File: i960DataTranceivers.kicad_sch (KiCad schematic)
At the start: 8 parts

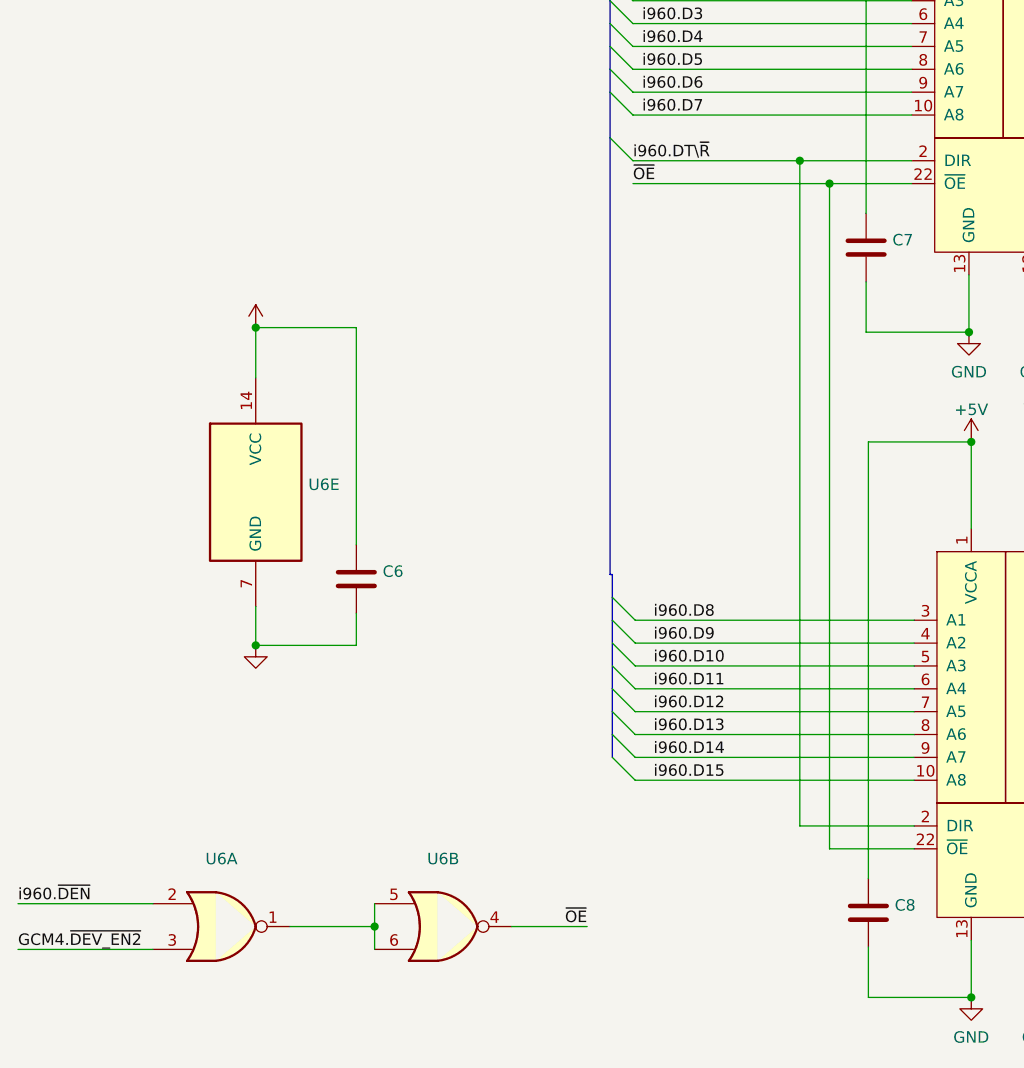
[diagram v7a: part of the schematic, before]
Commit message: Use a third 4809 running independently to act as glue and startup unit.
I was able to remove a nor gate ic by adding. I am also planning to use
the CCLs for other features as well. Perhaps as a simpler inverter.
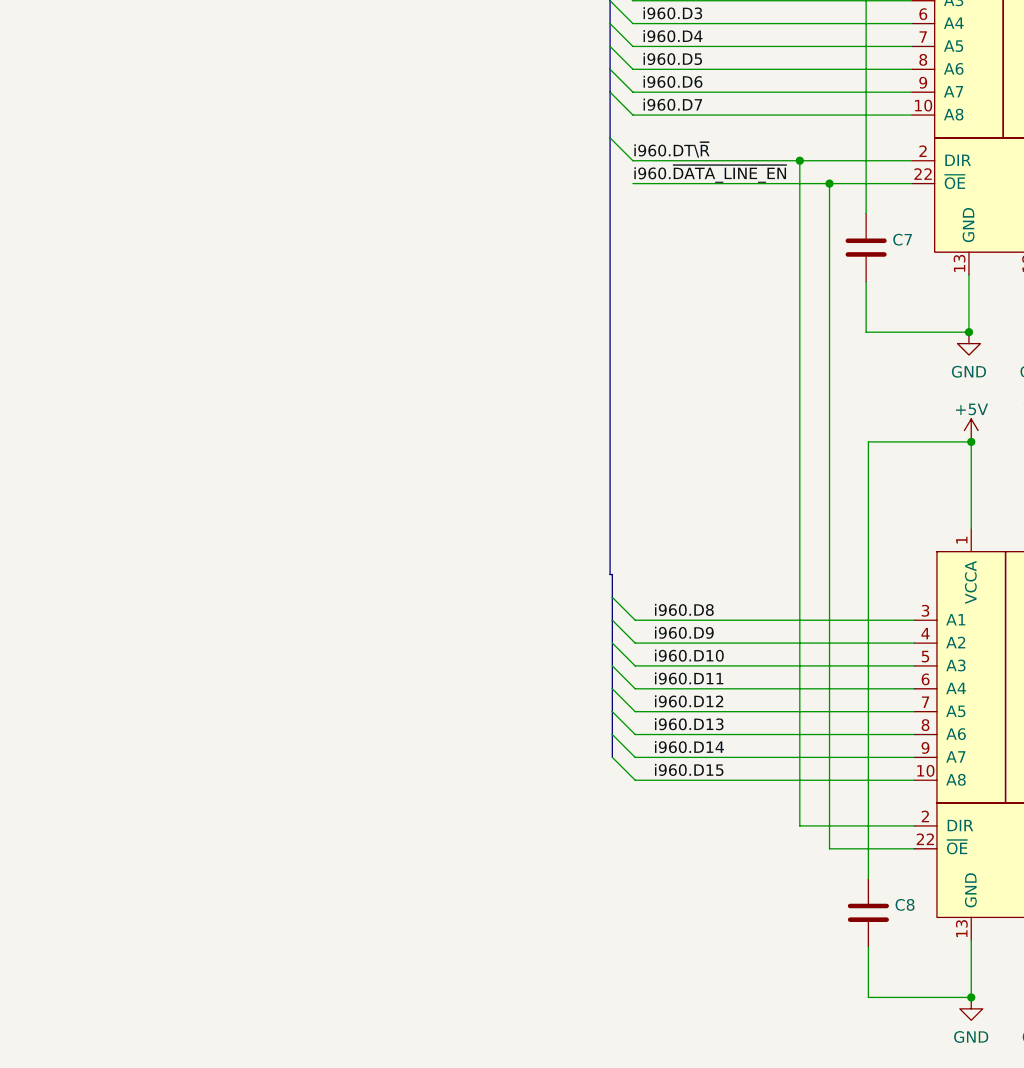
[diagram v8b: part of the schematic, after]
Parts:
- removed C6: (no value), symbol Device:C
- removed U6: (no value), symbol 74xx:74HC02
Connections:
- net ~{OE} renamed i960.~{DATA_LINE_EN}
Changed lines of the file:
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@@
   (junction (at 107.442 70.358) (diameter 0) (color 0 0 0 0)
   )
-  (junction (at 43.688 86.36) (diameter 0) (color 0 0 0 0)
-  )
   (junction (at 130.81 99.06) (diameter 0) (color 0 0 0 0)
   )
@@
   (junction (at 122.936 86.868) (diameter 0) (color 0 0 0 0)
   )
-  (junction (at 56.896 152.908) (diameter 0) (color 0 0 0 0)
-  )
   (junction (at 123.19 160.782) (diameter 0) (color 0 0 0 0)
   )
@@
   (junction (at 123.19 99.06) (diameter 0) (color 0 0 0 0)
   )
-  (junction (at 43.688 121.666) (diameter 0) (color 0 0 0 0)
-  )
   (junction (at 130.556 25.146) (diameter 0) (color 0 0 0 0)
   )
@@
     (stroke (width 0) (type default) (color 0 0 0 0))
   )
-  (wire (pts (xy 56.896 152.908) (xy 56.896 155.448))
-    (stroke (width 0) (type default) (color 0 0 0 0))
-  )
-  (wire (pts (xy 54.864 118.11) (xy 54.864 121.666))
-    (stroke (width 0) (type default) (color 0 0 0 0))
-  )
   (wire (pts (xy 141.732 160.782) (xy 130.81 160.782))
     (stroke (width 0) (type default) (color 0 0 0 0))
@@
     (stroke (width 0) (type default) (color 0 0 0 0))
   )
-  (wire (pts (xy 56.896 152.908) (xy 56.896 150.368))
-    (stroke (width 0) (type default) (color 0 0 0 0))
-  )
   (wire (pts (xy 141.732 99.06) (xy 141.732 147.574))
     (stroke (width 0) (type default) (color 0 0 0 0))
   )
-  (wire (pts (xy 47.498 152.908) (xy 56.896 152.908))
-    (stroke (width 0) (type default) (color 0 0 0 0))
-  )
   (bus (pts (xy 83.058 42.418) (xy 83.058 44.958))
     (stroke (width 0) (type default) (color 0 0 0 0))
@@
     (stroke (width 0) (type default) (color 0 0 0 0))
   )
-  (wire (pts (xy 72.136 152.908) (xy 80.518 152.908))
-    (stroke (width 0) (type default) (color 0 0 0 0))
-  )
   (wire (pts (xy 107.442 70.358) (xy 116.586 70.358))
     (stroke (width 0) (type default) (color 0 0 0 0))
@@
     (stroke (width 0) (type default) (color 0 0 0 0))
   )
-  (wire (pts (xy 54.864 86.36) (xy 54.864 110.49))
-    (stroke (width 0) (type default) (color 0 0 0 0))
-  )
   (wire (pts (xy 137.16 131.572) (xy 168.148 131.572))
     (stroke (width 0) (type default) (color 0 0 0 0))
@@
     (stroke (width 0) (type default) (color 0 0 0 0))
   )
-  (wire (pts (xy 43.688 86.36) (xy 54.864 86.36))
-    (stroke (width 0) (type default) (color 0 0 0 0))
-  )
   (wire (pts (xy 123.19 154.432) (xy 123.19 160.782))
     (stroke (width 0) (type default) (color 0 0 0 0))
@@
     (stroke (width 0) (type default) (color 0 0 0 0))
   )
-  (wire (pts (xy 43.688 91.948) (xy 43.688 86.36))
-    (stroke (width 0) (type default) (color 0 0 0 0))
-  )
   (wire (pts (xy 123.19 99.06) (xy 123.19 108.712))
     (stroke (width 0) (type default) (color 0 0 0 0))
@@
     (stroke (width 0) (type default) (color 0 0 0 0))
   )
-  (wire (pts (xy 17.272 155.448) (xy 32.258 155.448))
-    (stroke (width 0) (type default) (color 0 0 0 0))
-  )
-  (wire (pts (xy 43.688 121.666) (xy 43.688 117.348))
-    (stroke (width 0) (type default) (color 0 0 0 0))
-  )
-  (wire (pts (xy 54.864 121.666) (xy 43.688 121.666))
-    (stroke (width 0) (type default) (color 0 0 0 0))
-  )
   (bus (pts (xy 83.058 57.658) (xy 83.058 60.198))
     (stroke (width 0) (type default) (color 0 0 0 0))
@@
   )
   (bus (pts (xy 83.312 116.332) (xy 83.312 118.872))
-    (stroke (width 0) (type default) (color 0 0 0 0))
-  )
-  (wire (pts (xy 17.272 150.368) (xy 32.258 150.368))
     (stroke (width 0) (type default) (color 0 0 0 0))
   )
@@
     (effects (font (size 1.27 1.27)) (justify right bottom))
   )
-  (label "~{OE}" (at 80.518 152.908 180)
-    (effects (font (size 1.27 1.27)) (justify right bottom))
+  (label "i960.~{DATA_LINE_EN}" (at 85.598 70.358 0)
+    (effects (font (size 1.27 1.27)) (justify left bottom))
   )
   (label "GCM4.L7" (at 167.894 62.738 180)
@@
     (effects (font (size 1.27 1.27)) (justify right bottom))
   )
-  (label "GCM4.~{DEV_EN2}" (at 17.272 155.448 0)
-    (effects (font (size 1.27 1.27)) (justify left bottom))
-  )
   (label "GCM4.L2" (at 167.894 50.038 180)
     (effects (font (size 1.27 1.27)) (justify right bottom))
@@
   )
   (label "i960.D10" (at 87.884 123.952 0)
-    (effects (font (size 1.27 1.27)) (justify left bottom))
-  )
-  (label "~{OE}" (at 85.598 70.358 0)
-    (effects (font (size 1.27 1.27)) (justify left bottom))
-  )
-  (label "i960.~{DEN}" (at 17.272 150.368 0)
     (effects (font (size 1.27 1.27)) (justify left bottom))
   )
@@
     (pin "1")
   )
-  (symbol (lib_id "74xx:74HC02") (at 64.516 152.908 0) (unit 2)
-    (in_bom yes) (on_board yes) (fields_autoplaced)
-    (property "Reference" "U6" (id 0) (at 64.516 145.3982 0))
-    (property "Value" "" (id 1) (at 64.516 147.9351 0))
-    (property "Footprint" "" (id 2) (at 64.516 152.908 0)
-      (effects (font (size 1.27 1.27)) hide)
-    )
-    (property "Datasheet" "http://www.ti.com/lit/gpn/sn74hc02" (id 3) (at 64.516 152.908 0)
-      (effects (font (size 1.27 1.27)) hide)
-    )
-    (pin "1")
-    (pin "2")
-    (pin "3")
-    (pin "4")
-    (pin "5")
-    (pin "6")
-    (pin "10")
-    (pin "8")
-    (pin "9")
-    (pin "11")
-    (pin "12")
-    (pin "13")
-    (pin "14")
-    (pin "7")
-  )
   (symbol (lib_id "Device:C") (at 141.732 151.384 0) (unit 1)
     (in_bom yes) (on_board yes) (fields_autoplaced)
@@
     )
     (property "Datasheet" "" (id 3) (at 123.19 160.782 0)
-      (effects (font (size 1.27 1.27)) hide)
-    )
-    (pin "1")
-  )
-  (symbol (lib_id "power:GND") (at 43.688 121.666 0) (unit 1)
-    (in_bom yes) (on_board yes) (fields_autoplaced)
-    (property "Reference" "#PWR0125" (id 0) (at 43.688 128.016 0)
-      (effects (font (size 1.27 1.27)) hide)
-    )
-    (property "Value" "" (id 1) (at 43.688 126.1094 0))
-    (property "Footprint" "" (id 2) (at 43.688 121.666 0)
-      (effects (font (size 1.27 1.27)) hide)
-    )
-    (property "Datasheet" "" (id 3) (at 43.688 121.666 0)
       (effects (font (size 1.27 1.27)) hide)
     )
@@
     (pin "9")
   )
-  (symbol (lib_id "74xx:74HC02") (at 39.878 152.908 0) (unit 1)
-    (in_bom yes) (on_board yes) (fields_autoplaced)
-    (property "Reference" "U6" (id 0) (at 39.878 145.3982 0))
-    (property "Value" "" (id 1) (at 39.878 147.9351 0))
-    (property "Footprint" "" (id 2) (at 39.878 152.908 0)
-      (effects (font (size 1.27 1.27)) hide)
-    )
-    (property "Datasheet" "http://www.ti.com/lit/gpn/sn74hc02" (id 3) (at 39.878 152.908 0)
+  (symbol (lib_id "Device:C") (at 111.506 77.47 0) (unit 1)
+    (in_bom yes) (on_board yes) (fields_autoplaced)
+    (property "Reference" "C7" (id 0) (at 114.427 76.6353 0)
+      (effects (font (size 1.27 1.27)) (justify left))
+    )
+    (property "Value" "" (id 1) (at 114.427 79.1722 0)
+      (effects (font (size 1.27 1.27)) (justify left))
+    )
+    (property "Footprint" "" (id 2) (at 112.4712 81.28 0)
+      (effects (font (size 1.27 1.27)) hide)
+    )
+    (property "Datasheet" "~" (id 3) (at 111.506 77.47 0)
       (effects (font (size 1.27 1.27)) hide)
     )
     (pin "1")
     (pin "2")
-    (pin "3")
-    (pin "4")
-    (pin "5")
-    (pin "6")
-    (pin "10")
-    (pin "8")
-    (pin "9")
-    (pin "11")
-    (pin "12")
-    (pin "13")
-    (pin "14")
-    (pin "7")
-  )
-  (symbol (lib_id "Device:C") (at 111.506 77.47 0) (unit 1)
-    (in_bom yes) (on_board yes) (fields_autoplaced)
-    (property "Reference" "C7" (id 0) (at 114.427 76.6353 0)
-      (effects (font (size 1.27 1.27)) (justify left))
-    )
-    (property "Value" "" (id 1) (at 114.427 79.1722 0)
-      (effects (font (size 1.27 1.27)) (justify left))
-    )
-    (property "Footprint" "" (id 2) (at 112.4712 81.28 0)
-      (effects (font (size 1.27 1.27)) hide)
-    )
-    (property "Datasheet" "~" (id 3) (at 111.506 77.47 0)
-      (effects (font (size 1.27 1.27)) hide)
-    )
-    (pin "1")
-    (pin "2")
-  )
-  (symbol (lib_id "74xx:74HC02") (at 43.688 104.648 0) (unit 5)
-    (in_bom yes) (on_board yes) (fields_autoplaced)
-    (property "Reference" "U6" (id 0) (at 49.53 103.8133 0)
-      (effects (font (size 1.27 1.27)) (justify left))
-    )
-    (property "Value" "" (id 1) (at 49.53 106.3502 0)
-      (effects (font (size 1.27 1.27)) (justify left))
-    )
-    (property "Footprint" "" (id 2) (at 43.688 104.648 0)
-      (effects (font (size 1.27 1.27)) hide)
-    )
-    (property "Datasheet" "http://www.ti.com/lit/gpn/sn74hc02" (id 3) (at 43.688 104.648 0)
-      (effects (font (size 1.27 1.27)) hide)
-    )
-    (pin "1")
-    (pin "2")
-    (pin "3")
-    (pin "4")
-    (pin "5")
-    (pin "6")
-    (pin "10")
-    (pin "8")
-    (pin "9")
-    (pin "11")
-    (pin "12")
-    (pin "13")
-    (pin "14")
-    (pin "7")
-  )
-  (symbol (lib_id "power:+5V") (at 43.688 86.36 0) (unit 1)
-    (in_bom yes) (on_board yes) (fields_autoplaced)
-    (property "Reference" "#PWR0126" (id 0) (at 43.688 90.17 0)
-      (effects (font (size 1.27 1.27)) hide)
-    )
-    (property "Value" "" (id 1) (at 43.688 82.7842 0))
-    (property "Footprint" "" (id 2) (at 43.688 86.36 0)
-      (effects (font (size 1.27 1.27)) hide)
-    )
-    (property "Datasheet" "" (id 3) (at 43.688 86.36 0)
-      (effects (font (size 1.27 1.27)) hide)
-    )
-    (pin "1")
   )
   (symbol (lib_id "power:VCC") (at 130.556 25.146 0) (unit 1)
@@
     (pin "1")
   )
-  (symbol (lib_id "Device:C") (at 54.864 114.3 0) (unit 1)
-    (in_bom yes) (on_board yes) (fields_autoplaced)
-    (property "Reference" "C6" (id 0) (at 57.785 113.4653 0)
-      (effects (font (size 1.27 1.27)) (justify left))
-    )
-    (property "Value" "" (id 1) (at 57.785 116.0022 0)
-      (effects (font (size 1.27 1.27)) (justify left))
-    )
-    (property "Footprint" "" (id 2) (at 55.8292 118.11 0)
-      (effects (font (size 1.27 1.27)) hide)
-    )
-    (property "Datasheet" "~" (id 3) (at 54.864 114.3 0)
-      (effects (font (size 1.27 1.27)) hide)
-    )
-    (pin "1")
-    (pin "2")
-  )
 )
